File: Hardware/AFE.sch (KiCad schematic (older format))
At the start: 38 parts, among them U801 4069.HEF4069UBTT,118, U802 MCP47CXBX2

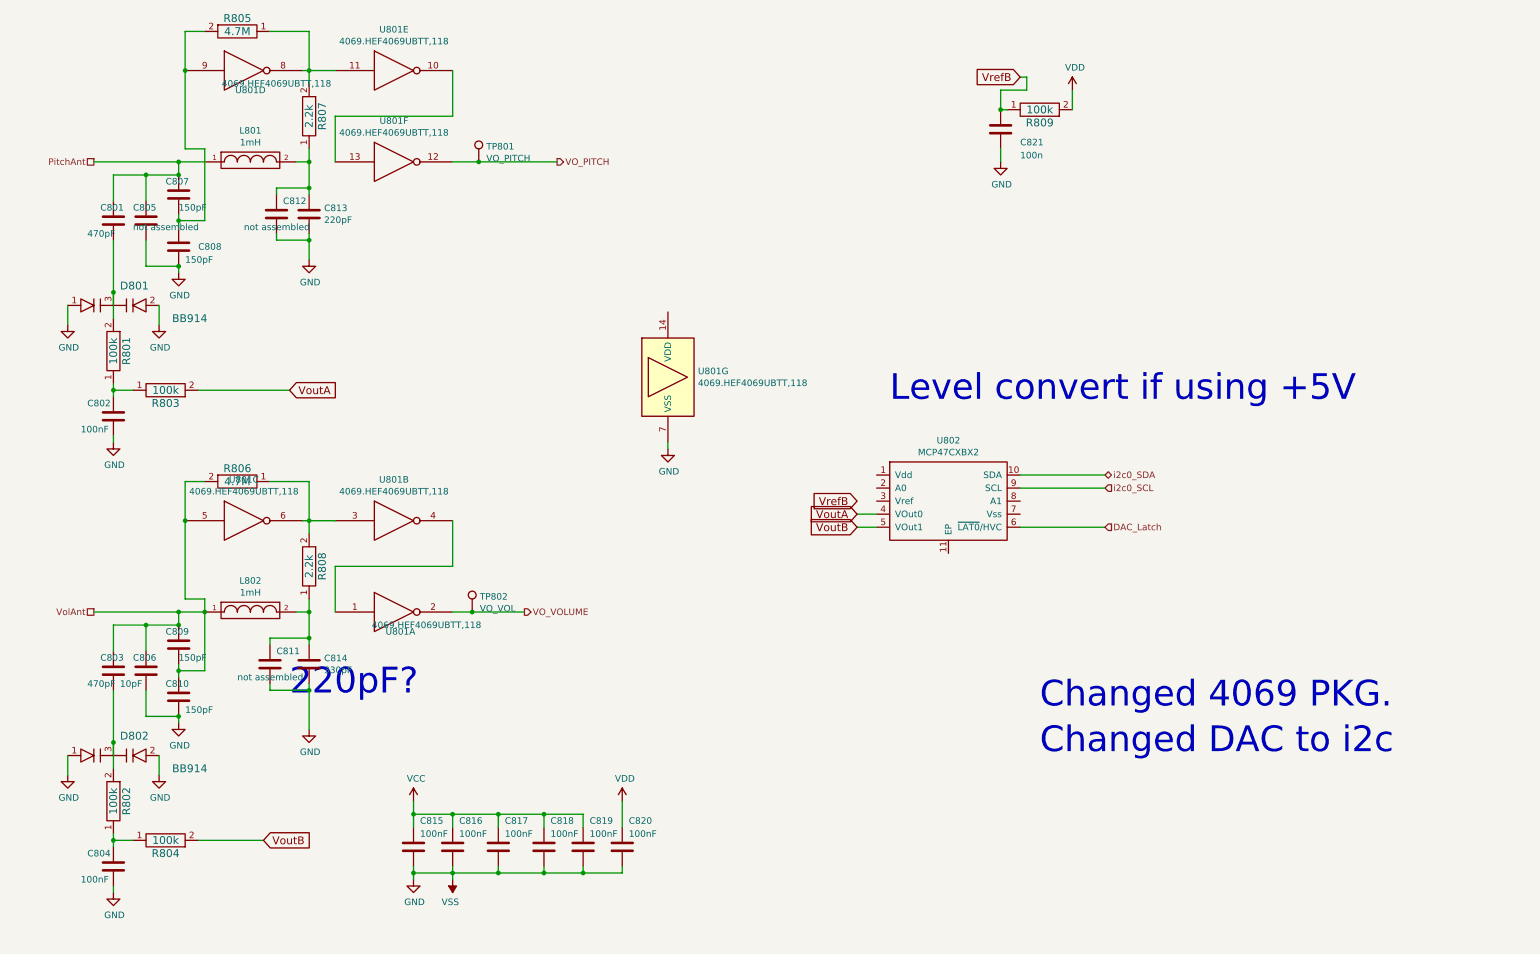
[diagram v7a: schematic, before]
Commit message: Option for tri-color reverse mount LED.
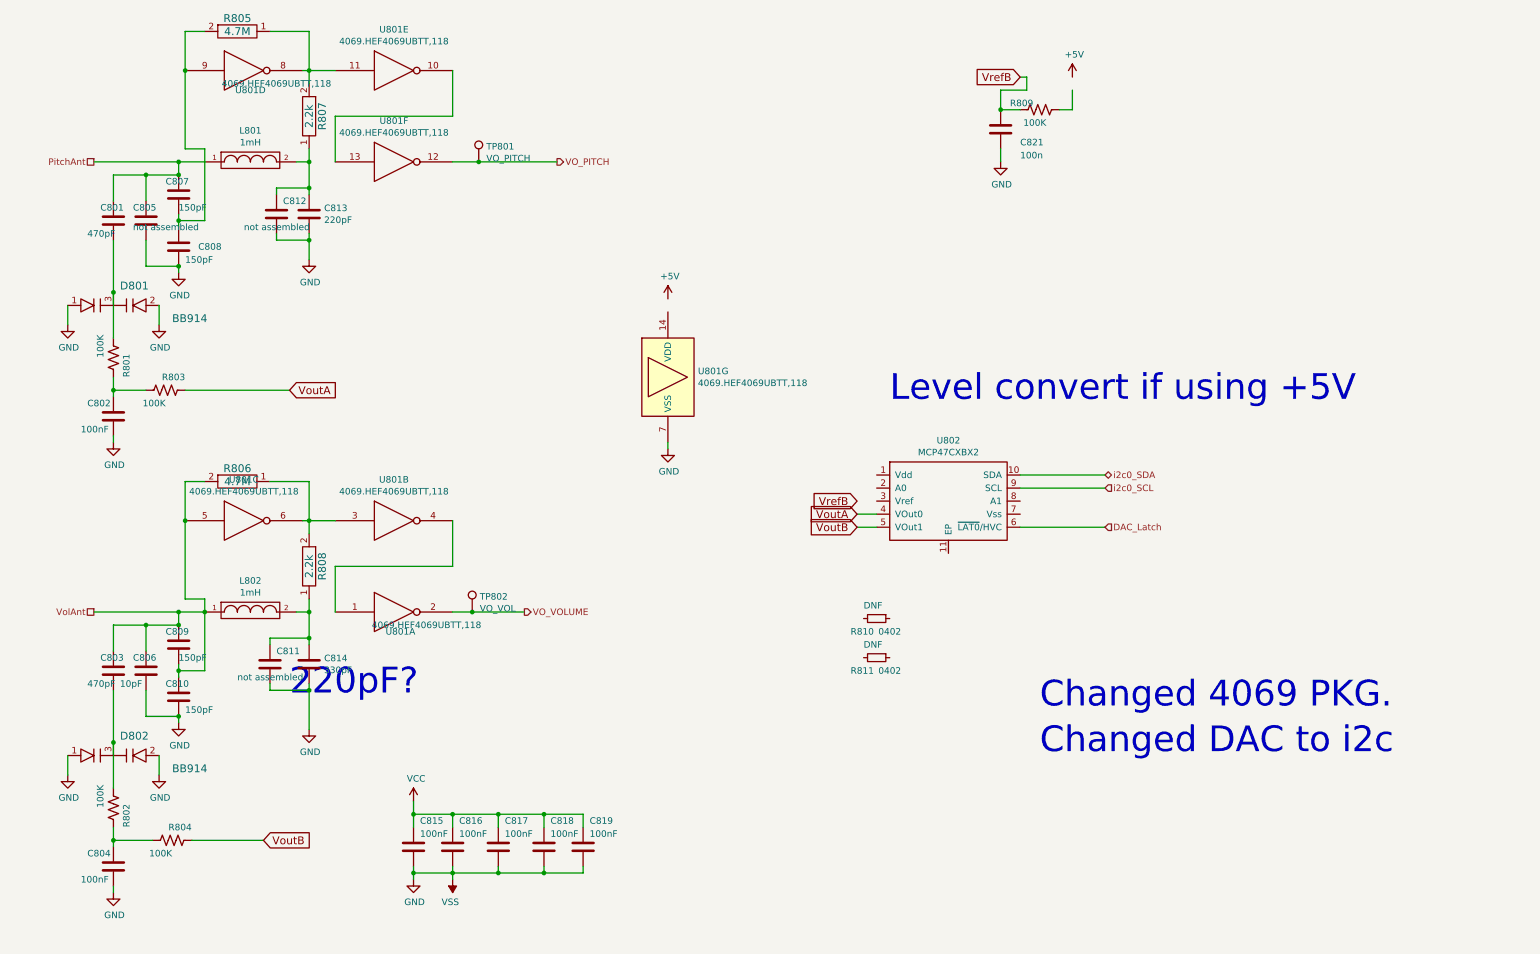
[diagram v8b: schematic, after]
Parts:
- removed C820: 100nF, Capacitor_SMD:C_0603_1608Metric_Pad1.08x0.95mm_HandSolder, symbol Device:C
- removed R801, R802, R804, R809: 100k, Resistor_SMD:R_0603_1608Metric_Pad0.98x0.95mm_HandSolder, symbol OpenThereminCC-rescue:RES
- removed R803: 100k, Capacitor_SMD:C_0603_1608Metric_Pad1.08x0.95mm_HandSolder, symbol OpenThereminCC-rescue:RES
- added R801, R802, R803, R804, R809: 100K, Resistor_SMD:R_0603_1608Metric, symbol Device:R_US
- added R810, R811: DNF, Resistor_SMD:R_0402_1005Metric, symbol Device:R_Small
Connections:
- net VoutA: now also R803.2
- net VoutB: now also R804.2
- net VrefB: now also R809.1
- net at C801.2, D801.3: now also R801.1
- net at C802.1: now also R801.2, R803.1
- net at C803.2, D802.3: now also R802.1
- net at C804.1: now also R802.2, R804.1
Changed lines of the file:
@@
-$EndComp
-$Comp
-L OpenThereminCC-rescue:RES R801
-U 1 1 571D9573
-P 1050 3250
-F 0 "R801" H 1050 3350 60  0000 C CNN
-F 1 "100k" H 1050 3250 60  0000 C CNN
-F 2 "Resistor_SMD:R_0603_1608Metric_Pad0.98x0.95mm_HandSolder" H 1000 3250 60  0001 C CNN
-F 3 "" H 1000 3250 60  0000 C CNN
-	1    1050 3250
-	0    1    1    0
 $EndComp
 $Comp
@@
 	1    1050 3750
 	1    0    0    -1
-$EndComp
-$Comp
-L OpenThereminCC-rescue:RES R803
-U 1 1 571D9C60
-P 1450 3550
-F 0 "R803" H 1450 3650 60  0000 C CNN
-F 1 "100k" H 1450 3550 60  0000 C CNN
-F 2 "Capacitor_SMD:C_0603_1608Metric_Pad1.08x0.95mm_HandSolder" H 1400 3550 60  0001 C CNN
-F 3 "" H 1400 3550 60  0000 C CNN
-	1    1450 3550
-	-1   0    0    1
 $EndComp
 $Comp
@@
 	1550 1900 1550 1800
 Connection ~ 1550 1800
-Wire Wire Line
-	1050 3500 1050 3550
-Wire Wire Line
-	1200 3550 1050 3550
 Connection ~ 1050 3550
 Wire Wire Line
@@
 	1550 5350 1550 5250
 Connection ~ 1550 5250
-Wire Wire Line
-	1050 6950 1050 7000
-Wire Wire Line
-	1200 7000 1050 7000
 Connection ~ 1050 7000
 Wire Wire Line
@@
 	3650 4900 3650 4550
 Wire Wire Line
-	1700 7000 2200 7000
-Wire Wire Line
 	2550 2350 2550 2400
-Wire Wire Line
-	1700 3550 2400 3550
 $Comp
 L Device:C C821
@@
 	1    0    0    -1
 $EndComp
-$Comp
-L OpenThereminCC-rescue:RES R809
-U 1 1 57213419
-P 8150 1400
-F 0 "R809" H 8150 1500 60  0000 C CNN
-F 1 "100k" H 8150 1400 60  0000 C CNN
-F 2 "Resistor_SMD:R_0603_1608Metric_Pad0.98x0.95mm_HandSolder" H 8100 1400 60  0001 C CNN
-F 3 "" H 8100 1400 60  0000 C CNN
-	1    8150 1400
-	-1   0    0    1
-$EndComp
-Wire Wire Line
-	7900 1400 7850 1400
 Wire Wire Line
 	7850 1400 7850 1250
@@
 	7850 1800 7850 1700
 Connection ~ 7850 1400
-$Comp
-L power:VDD #PWR0816
-U 1 1 57214AC2
-P 8400 1250
-F 0 "#PWR0816" H 8400 1100 50  0001 C CNN
-F 1 "VDD" H 8420 1423 50  0000 C CNN
-F 2 "" H 8400 1250 50  0000 C CNN
-F 3 "" H 8400 1250 50  0000 C CNN
-	1    8400 1250
-	1    0    0    -1
-$EndComp
 Wire Wire Line
 	8400 1250 8400 1400
@@
 $EndComp
 $Comp
-L Device:C C820
-U 1 1 57233688
-P 4950 7050
-F 0 "C820" H 5000 7250 50  0000 L CNN
-F 1 "100nF" H 5000 7150 50  0000 L CNN
-F 2 "Capacitor_SMD:C_0603_1608Metric_Pad1.08x0.95mm_HandSolder" H 4988 6900 50  0001 C CNN
-F 3 "" H 4950 7050 50  0000 C CNN
-	1    4950 7050
-	1    0    0    -1
-$EndComp
-$Comp
 L Device:C C815
 U 1 1 5723379F
@@
 	4650 7250 4650 7200
 Connection ~ 4350 7250
-Wire Wire Line
-	4950 7250 4950 7200
-Connection ~ 4650 7250
 $Comp
 L power:VCC #PWR0811
@@
 Connection ~ 4350 6800
 Wire Wire Line
-	4950 6700 4950 6900
-Wire Wire Line
 	2250 800  2550 800
 Wire Wire Line
@@
 Wire Wire Line
 	4650 6800 4650 6900
-$Comp
-L power:VDD #PWR0814
-U 1 1 572F3CCA
-P 4950 6700
-F 0 "#PWR0814" H 4950 6550 50  0001 C CNN
-F 1 "VDD" H 4970 6873 50  0000 C CNN
-F 2 "" H 4950 6700 50  0000 C CNN
-F 3 "" H 4950 6700 50  0000 C CNN
-	1    4950 6700
-	1    0    0    -1
-$EndComp
 $Comp
 L power:VSS #PWR0813
@@
 	1050 3550 1050 3600
 Wire Wire Line
-	1050 2800 1050 3000
-Wire Wire Line
 	2550 4550 2750 4550
 Wire Wire Line
@@
 Wire Wire Line
 	4350 7250 4650 7250
-Wire Wire Line
-	4650 7250 4950 7250
 Wire Wire Line
 	3350 6800 3350 6900
@@
 Text HLabel 8650 4600 2    50   Input ~ 0
 DAC_Latch
-$Comp
-L OpenThereminCC-rescue:RES R804
-U 1 1 571F644C
-P 1450 7000
-F 0 "R804" H 1450 7100 60  0000 C CNN
-F 1 "100k" H 1450 7000 60  0000 C CNN
-F 2 "Resistor_SMD:R_0603_1608Metric_Pad0.98x0.95mm_HandSolder" H 1400 7000 60  0001 C CNN
-F 3 "" H 1400 7000 60  0000 C CNN
-	1    1450 7000
-	-1   0    0    1
-$EndComp
-$Comp
-L OpenThereminCC-rescue:RES R802
-U 1 1 571F643F
-P 1050 6700
-F 0 "R802" H 1050 6800 60  0000 C CNN
-F 1 "100k" H 1050 6700 60  0000 C CNN
-F 2 "Resistor_SMD:R_0603_1608Metric_Pad0.98x0.95mm_HandSolder" H 1000 6700 60  0001 C CNN
-F 3 "" H 1000 6700 60  0000 C CNN
-	1    1050 6700
-	0    1    1    0
-$EndComp
 Wire Wire Line
 	1050 5850 1050 6250
@@
 $EndComp
 Connection ~ 1050 6250
-Wire Wire Line
-	1050 6250 1050 6450
 $Comp
 L OpenThereminCC-rescue:FILTER L802
@@
 Wire Wire Line
 	5300 4000 5300 3950
+$Comp
+L Device:R_Small R?
+U 1 1 615EAAD7
+P 6900 5300
+AR Path="/611E335F/615EAAD7" Ref="R?"  Part="1"
+AR Path="/615EAAD7" Ref="R?"  Part="1"
+AR Path="/611E3335/615EAAD7" Ref="R?"  Part="1"
+AR Path="/612429E8/615EAAD7" Ref="R810"  Part="1"
+F 0 "R810" V 7000 5100 50  0000 L CNN
+F 1 "DNF" V 6800 5200 50  0000 L CNN
+F 2 "Resistor_SMD:R_0402_1005Metric" V 6830 5300 50  0001 C CNN
+F 3 "~" H 6900 5300 50  0001 C CNN
+F 4 "0402" V 7000 5400 50  0000 C CNN "Pkg"
+F 5 "" H 6900 5300 50  0001 C CNN "MPN"
+F 6 "" H 6900 5300 50  0001 C CNN "DPN"
+	1    6900 5300
+	0    1    1    0
+$EndComp
+$Comp
+L Device:R_Small R?
+U 1 1 615EAAE0
+P 6900 5600
+AR Path="/611E335F/615EAAE0" Ref="R?"  Part="1"
+AR Path="/615EAAE0" Ref="R?"  Part="1"
+AR Path="/611E3335/615EAAE0" Ref="R?"  Part="1"
+AR Path="/612429E8/615EAAE0" Ref="R811"  Part="1"
+F 0 "R811" V 7000 5400 50  0000 L CNN
+F 1 "DNF" V 6800 5500 50  0000 L CNN
+F 2 "Resistor_SMD:R_0402_1005Metric" V 6830 5600 50  0001 C CNN
+F 3 "~" H 6900 5600 50  0001 C CNN
+F 4 "0402" V 7000 5700 50  0000 C CNN "Pkg"
+F 5 "" H 6900 5600 50  0001 C CNN "MPN"
+F 6 "" H 6900 5600 50  0001 C CNN "DPN"
+	1    6900 5600
+	0    1    1    0
+$EndComp
+$Comp
+L power:+5V #PWR?
+U 1 1 615F7BD2
+P 5300 2850
+AR Path="/6123BB15/615F7BD2" Ref="#PWR?"  Part="1"
+AR Path="/611E335F/615F7BD2" Ref="#PWR?"  Part="1"
+AR Path="/612429E8/615F7BD2" Ref="#PWR0143"  Part="1"
+F 0 "#PWR0143" H 5300 2700 50  0001 C CNN
+F 1 "+5V" H 5315 3023 50  0000 C CNN
+F 2 "" H 5300 2850 50  0001 C CNN
+F 3 "" H 5300 2850 50  0001 C CNN
+	1    5300 2850
+	1    0    0    -1
+$EndComp
+$Comp
+L power:+5V #PWR?
+U 1 1 61614765
+P 8400 1150
+AR Path="/6123BB15/61614765" Ref="#PWR?"  Part="1"
+AR Path="/611E335F/61614765" Ref="#PWR?"  Part="1"
+AR Path="/612429E8/61614765" Ref="#PWR0144"  Part="1"
+F 0 "#PWR0144" H 8400 1000 50  0001 C CNN
+F 1 "+5V" H 8415 1323 50  0000 C CNN
+F 2 "" H 8400 1150 50  0001 C CNN
+F 3 "" H 8400 1150 50  0001 C CNN
+	1    8400 1150
+	1    0    0    -1
+$EndComp
+$Comp
+L Device:R_US R?
+U 1 1 61624C4C
+P 1450 3550
+AR Path="/611E335F/61624C4C" Ref="R?"  Part="1"
+AR Path="/612429E8/61624C4C" Ref="R803"  Part="1"
+F 0 "R803" V 1550 3400 50  0000 L CNN
+F 1 "100K" V 1350 3550 50  0000 L CNN
+F 2 "Resistor_SMD:R_0603_1608Metric" V 1380 3550 50  0001 C CNN
+F 3 "~" H 1450 3550 50  0001 C CNN
+F 4 "0603" H 1450 3550 50  0001 C CNN "Pkg"
+F 5 "ESR03EZPJ104" H 1450 3550 50  0001 C CNN "MPN"
+F 6 "RHM100KDCT-ND" H 1450 3550 50  0001 C CNN "DPN"
+	1    1450 3550
+	0    -1   -1   0
+$EndComp
+Wire Wire Line
+	1600 3550 2400 3550
+Wire Wire Line
+	1050 3550 1300 3550
+$Comp
+L Device:R_US R?
+U 1 1 6163B087
+P 1050 3300
+AR Path="/611E335F/6163B087" Ref="R?"  Part="1"
+AR Path="/612429E8/6163B087" Ref="R801"  Part="1"
+F 0 "R801" V 1150 3150 50  0000 L CNN
+F 1 "100K" V 950 3300 50  0000 L CNN
+F 2 "Resistor_SMD:R_0603_1608Metric" V 980 3300 50  0001 C CNN
+F 3 "~" H 1050 3300 50  0001 C CNN
+F 4 "0603" H 1050 3300 50  0001 C CNN "Pkg"
+F 5 "ESR03EZPJ104" H 1050 3300 50  0001 C CNN "MPN"
+F 6 "RHM100KDCT-ND" H 1050 3300 50  0001 C CNN "DPN"
+	1    1050 3300
+	1    0    0    -1
+$EndComp
+Wire Wire Line
+	1050 2800 1050 3150
+Wire Wire Line
+	1050 3450 1050 3550
+$Comp
+L Device:R_US R?
+U 1 1 616468EF
+P 8150 1400
+AR Path="/611E335F/616468EF" Ref="R?"  Part="1"
+AR Path="/612429E8/616468EF" Ref="R809"  Part="1"
+F 0 "R809" V 8200 1450 50  0000 L CNN
+F 1 "100K" V 8050 1350 50  0000 L CNN
+F 2 "Resistor_SMD:R_0603_1608Metric" V 8080 1400 50  0001 C CNN
+F 3 "~" H 8150 1400 50  0001 C CNN
+F 4 "0603" H 8150 1400 50  0001 C CNN "Pkg"
+F 5 "ESR03EZPJ104" H 8150 1400 50  0001 C CNN "MPN"
+F 6 "RHM100KDCT-ND" H 8150 1400 50  0001 C CNN "DPN"
+	1    8150 1400
+	0    -1   -1   0
+$EndComp
+Wire Wire Line
+	8400 1400 8300 1400
+Wire Wire Line
+	7850 1400 8000 1400
+$Comp
+L Device:R_US R?
+U 1 1 6165DF0B
+P 1500 7000
+AR Path="/611E335F/6165DF0B" Ref="R?"  Part="1"
+AR Path="/612429E8/6165DF0B" Ref="R804"  Part="1"
+F 0 "R804" V 1600 6850 50  0000 L CNN
+F 1 "100K" V 1400 7000 50  0000 L CNN
+F 2 "Resistor_SMD:R_0603_1608Metric" V 1430 7000 50  0001 C CNN
+F 3 "~" H 1500 7000 50  0001 C CNN
+F 4 "0603" H 1500 7000 50  0001 C CNN "Pkg"
+F 5 "ESR03EZPJ104" H 1500 7000 50  0001 C CNN "MPN"
+F 6 "RHM100KDCT-ND" H 1500 7000 50  0001 C CNN "DPN"
+	1    1500 7000
+	0    -1   -1   0
+$EndComp
+Wire Wire Line
+	1650 7000 2200 7000
+Wire Wire Line
+	1050 7000 1350 7000
+$Comp
+L Device:R_US R?
+U 1 1 6166C1B1
+P 1050 6750
+AR Path="/611E335F/6166C1B1" Ref="R?"  Part="1"
+AR Path="/612429E8/6166C1B1" Ref="R802"  Part="1"
+F 0 "R802" V 1150 6600 50  0000 L CNN
+F 1 "100K" V 950 6750 50  0000 L CNN
+F 2 "Resistor_SMD:R_0603_1608Metric" V 980 6750 50  0001 C CNN
+F 3 "~" H 1050 6750 50  0001 C CNN
+F 4 "0603" H 1050 6750 50  0001 C CNN "Pkg"
+F 5 "ESR03EZPJ104" H 1050 6750 50  0001 C CNN "MPN"
+F 6 "RHM100KDCT-ND" H 1050 6750 50  0001 C CNN "DPN"
+	1    1050 6750
+	1    0    0    -1
+$EndComp
+Wire Wire Line
+	1050 6250 1050 6600
+Wire Wire Line
+	1050 6900 1050 7000
 $EndSCHEMATC
